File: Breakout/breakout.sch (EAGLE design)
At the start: 57 parts, among them Q1 16Mhz, U1 TPS63001DRCT, U11 XL

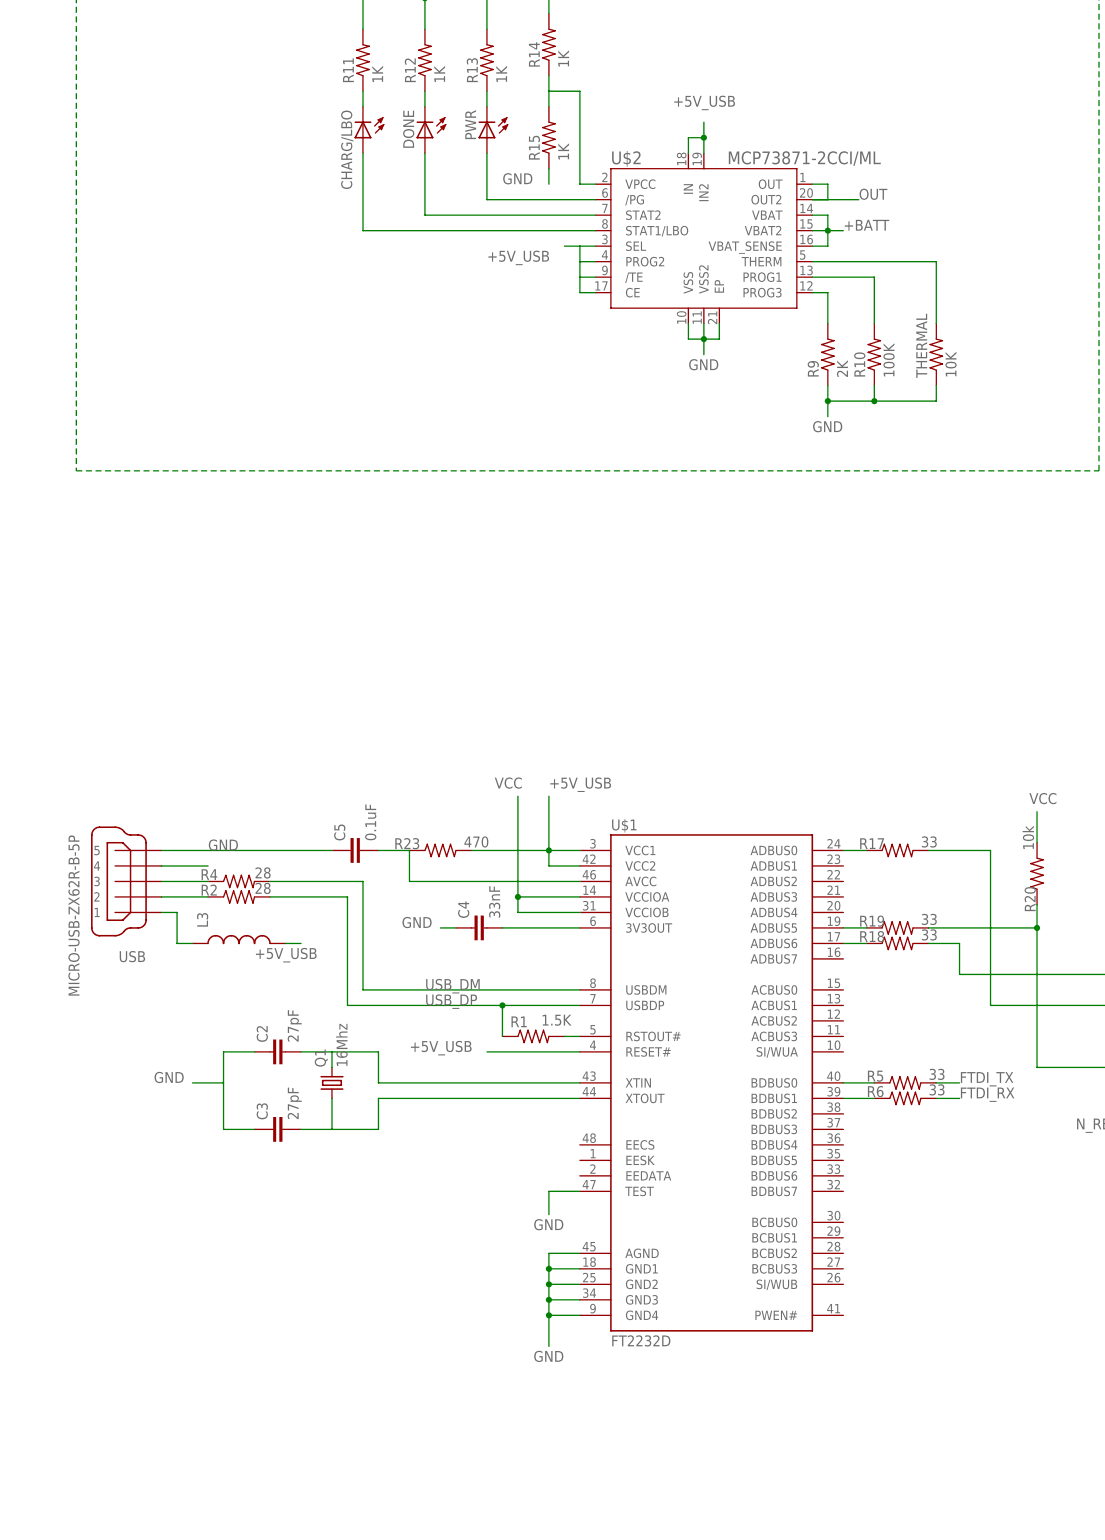
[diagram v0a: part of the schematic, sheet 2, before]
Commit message: Added EEPROM for FTDI chip
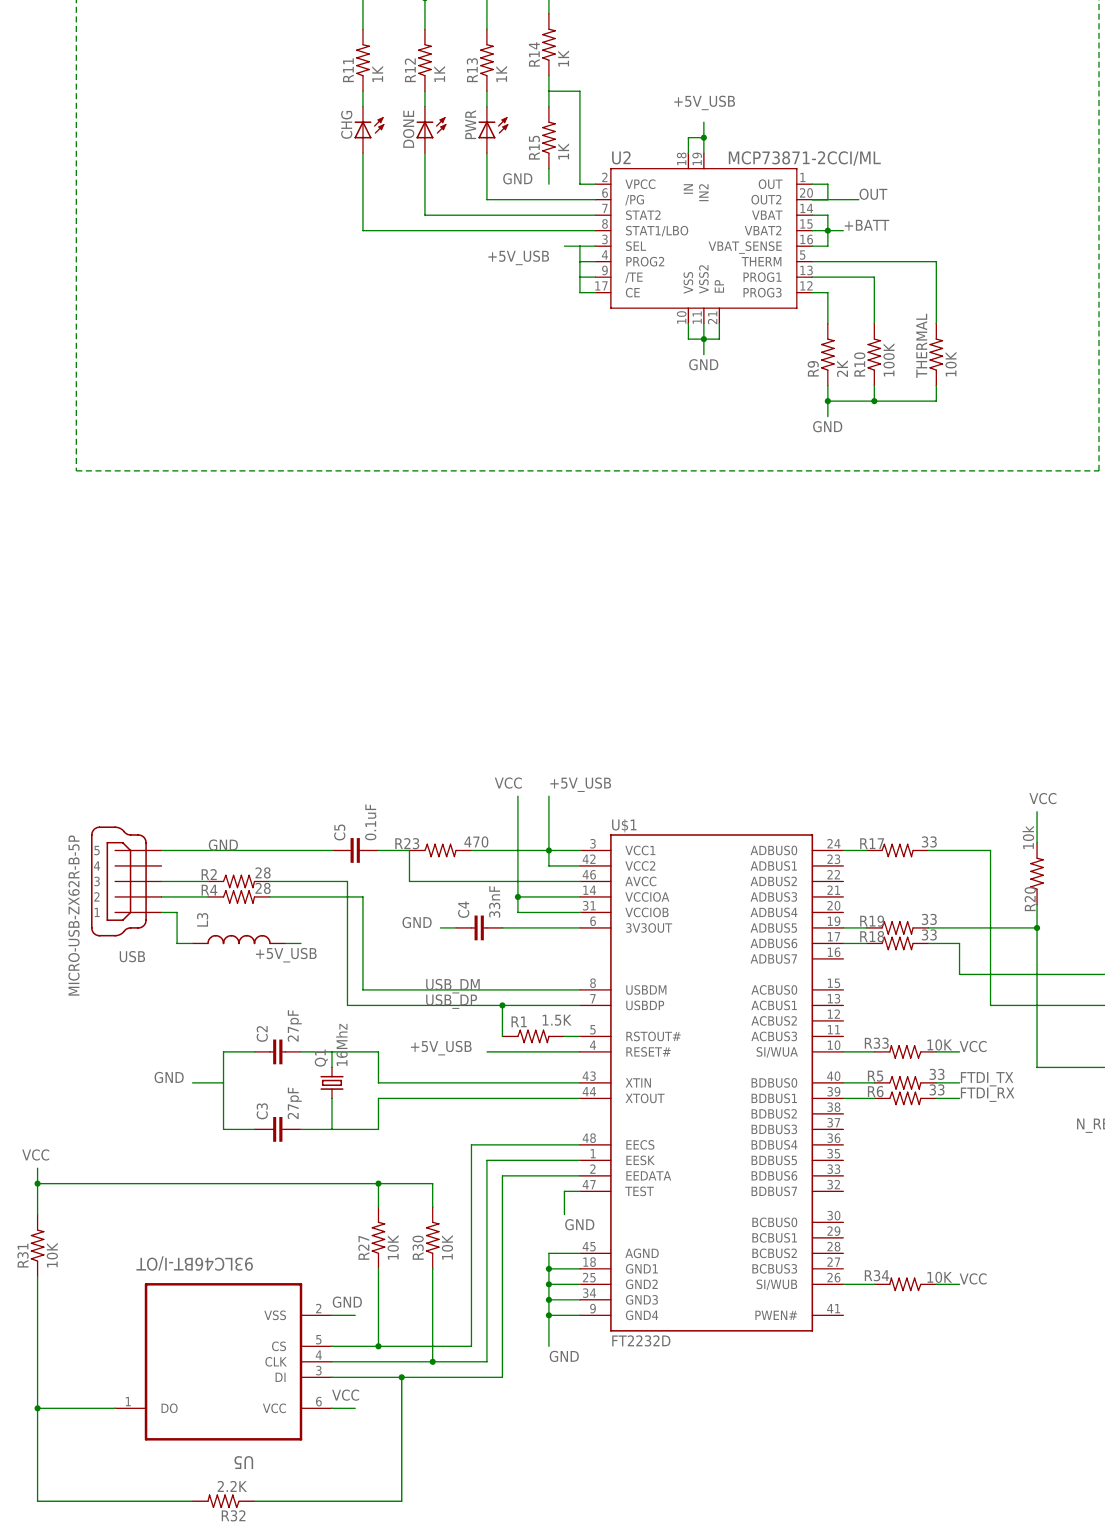
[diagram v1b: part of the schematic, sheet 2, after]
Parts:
- added R27, R30, R31, R33, R34: 10K, SparkFun-Passives:RESISTOR0402-RES
- added R32: 2.2K, SparkFun-Passives:RESISTOR0402-RES
- added U5: 93LC46BT-I/OT, Microchip_By_element14_Batch_1:93LC46BT-I/OT
- renumbered CHARG/LBO to CHG, U$2 to U2
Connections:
- new net N$16: R4.1, USB.2
- new net N$24: R2.1, USB.3
- new net N$54: R31.1, R32.2, U5.DO
- new net N$55: R33.2, U$1.SI/WUA
- new net N$56: R34.2, U$1.SI/WUB
- net GND: now also U5.VSS
- net N$39: now also R27.1, U$1.EECS, U5.CS; no longer USB.4
- net N$41: now also R30.1, U$1.EESK, U5.CLK; no longer R4.1, USB.3
- net N$42: now also R32.1, U$1.EEDATA, U5.DI; no longer R2.1, USB.2
- net VCC: now also R27.2, R30.2, R31.2, R33.1, U5.VCC
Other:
- moved on the sheet: R2, R4

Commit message: Temp Sensor added
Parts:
- added C7: .1uF, SparkFun-Capacitors:CAP0402-CAP
- added R35, R37: 0R, SparkFun-Passives:RESISTOR0603-RES
- added R36: 33K, SparkFun-Passives:RESISTOR0402-RES
- added U12: TMP006, SparkFun-DigitalIC:TMP006
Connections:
- new net GPIO_30: CC3200MOD.42_GPIO30, R35.1, U11.GPIO_30
- new net N$57: R35.2, R36.1, U12.!DRDY
- net GND: now also C7.1, U12.ADR0, U12.AGND, U12.DGND
- net GPIO_10: now also U12.SCL
- net GPIO_11: now also U12.SDA
- net N$14: now also C7.2, R36.2, R37.2, U12.ADR1, U12.V+; no longer CC3200MOD.42_GPIO30, U11.GPIO_30
- net VCC: now also R37.1
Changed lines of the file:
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@@
 <part name="R33" library="SparkFun-Passives" deviceset="RESISTOR" device="0402-RES" value="10K"/>
 <part name="R34" library="SparkFun-Passives" deviceset="RESISTOR" device="0402-RES" value="10K"/>
+<part name="U12" library="SparkFun-DigitalIC" deviceset="TMP006" device=""/>
+<part name="R35" library="SparkFun-Passives" deviceset="RESISTOR" device="0603-RES" value="0R"/>
+<part name="R36" library="SparkFun-Passives" deviceset="RESISTOR" device="0402-RES" value="33K"/>
+<part name="R37" library="SparkFun-Passives" deviceset="RESISTOR" device="0603-RES" value="0R"/>
+<part name="C7" library="SparkFun-Capacitors" deviceset="CAP" device="0402-CAP" value=".1uF"/>
 </parts>
 <sheets>
@@
 </segment>
 </net>
-<net name="N$14" class="0">
+<net name="GPIO_30" class="0">
 <segment>
 <pinref part="CC3200MOD" gate="G$1" pin="42_GPIO30"/>
@@
 <attribute name="VALUE" x="165.1" y="286.512" size="1.778" layer="96" rot="R180"/>
 </instance>
+<instance part="U12" gate="G$1" x="508" y="347.98" rot="R180"/>
+<instance part="R35" gate="G$1" x="469.9" y="340.36" rot="R90"/>
+<instance part="R36" gate="G$1" x="459.74" y="339.09" rot="R270"/>
+<instance part="R37" gate="G$1" x="532.13" y="342.9" rot="R180"/>
+<instance part="C7" gate="G$1" x="472.44" y="363.22" rot="R270"/>
 </instances>
 <busses>
@@
 <wire x1="63.5" y1="279.4" x2="67.31" y2="279.4" width="0.1524" layer="91"/>
 <label x="63.5" y="280.67" size="1.778" layer="95"/>
+</segment>
+<segment>
+<pinref part="U12" gate="G$1" pin="AGND"/>
+<wire x1="523.24" y1="353.06" x2="525.78" y2="353.06" width="0.1524" layer="91"/>
+<wire x1="525.78" y1="353.06" x2="525.78" y2="350.52" width="0.1524" layer="91"/>
+<wire x1="525.78" y1="350.52" x2="530.86" y2="350.52" width="0.1524" layer="91"/>
+<pinref part="U12" gate="G$1" pin="DGND"/>
+<wire x1="525.78" y1="350.52" x2="523.24" y2="350.52" width="0.1524" layer="91"/>
+<label x="530.86" y="350.52" size="1.778" layer="95"/>
+<junction x="525.78" y="350.52"/>
+</segment>
+<segment>
+<pinref part="U12" gate="G$1" pin="ADR0"/>
+<label x="482.6" y="353.06" size="1.778" layer="95"/>
+<wire x1="492.76" y1="353.06" x2="481.33" y2="353.06" width="0.1524" layer="91"/>
+<wire x1="481.33" y1="353.06" x2="481.33" y2="363.22" width="0.1524" layer="91"/>
+<pinref part="C7" gate="G$1" pin="1"/>
+<wire x1="481.33" y1="363.22" x2="477.52" y2="363.22" width="0.1524" layer="91"/>
 </segment>
 </net>
@@
 <label x="166.37" y="284.48" size="1.778" layer="95"/>
 </segment>
+<segment>
+<pinref part="R37" gate="G$1" pin="1"/>
+<wire x1="537.21" y1="342.9" x2="543.56" y2="342.9" width="0.1524" layer="91"/>
+<label x="543.56" y="342.9" size="1.778" layer="95"/>
+</segment>
 </net>
 <net name="N$9" class="0">
@@
 <pinref part="U$3" gate="G$1" pin="OE2"/>
 <wire x1="179.07" y1="320.04" x2="217.17" y2="320.04" width="0.1524" layer="91"/>
-<label x="191.77" y="342.9" size="1.778" layer="95"/>
+<label x="181.61" y="342.9" size="1.778" layer="95"/>
 <junction x="179.07" y="342.9"/>
 </segment>
@@
 <segment>
 <pinref part="R25" gate="G$1" pin="1"/>
-<wire x1="397.51" y1="307.34" x2="397.51" y2="302.26" width="0.1524" layer="91"/>
+<wire x1="397.51" y1="307.34" x2="397.51" y2="304.8" width="0.1524" layer="91"/>
 <label x="392.43" y="298.45" size="1.778" layer="95"/>
+<wire x1="397.51" y1="304.8" x2="397.51" y2="302.26" width="0.1524" layer="91"/>
+<wire x1="397.51" y1="309.88" x2="397.51" y2="304.8" width="0.1524" layer="91"/>
 </segment>
 </net>
@@
 <wire x1="440.69" y1="372.11" x2="440.69" y2="361.95" width="0.1524" layer="91"/>
 <label x="434.34" y="359.41" size="1.778" layer="95"/>
+</segment>
+<segment>
+<pinref part="U12" gate="G$1" pin="SCL"/>
+<wire x1="492.76" y1="342.9" x2="487.68" y2="342.9" width="0.1524" layer="91"/>
+<label x="477.52" y="342.9" size="1.778" layer="95"/>
 </segment>
 </net>
@@
 <wire x1="454.66" y1="369.57" x2="454.66" y2="361.95" width="0.1524" layer="91"/>
 <label x="450.85" y="359.41" size="1.778" layer="95"/>
+</segment>
+<segment>
+<pinref part="U12" gate="G$1" pin="SDA"/>
+<wire x1="492.76" y1="345.44" x2="487.68" y2="345.44" width="0.1524" layer="91"/>
+<label x="477.52" y="345.44" size="1.778" layer="95"/>
 </segment>
 </net>
@@
 </segment>
 </net>
+<net name="N$57" class="0">
+<segment>
+<pinref part="U12" gate="G$1" pin="!DRDY"/>
+<wire x1="492.76" y1="347.98" x2="469.9" y2="347.98" width="0.1524" layer="91"/>
+<wire x1="469.9" y1="347.98" x2="469.9" y2="345.44" width="0.1524" layer="91"/>
+<pinref part="R35" gate="G$1" pin="2"/>
+<pinref part="R36" gate="G$1" pin="1"/>
+<wire x1="469.9" y1="347.98" x2="459.74" y2="347.98" width="0.1524" layer="91"/>
+<wire x1="459.74" y1="347.98" x2="459.74" y2="344.17" width="0.1524" layer="91"/>
+<junction x="469.9" y="347.98"/>
+</segment>
+</net>
+<net name="GPIO_30" class="0">
+<segment>
+<pinref part="R35" gate="G$1" pin="1"/>
+<wire x1="469.9" y1="335.28" x2="469.9" y2="330.2" width="0.1524" layer="91"/>
+<label x="464.82" y="327.66" size="1.778" layer="95"/>
+</segment>
+</net>
+<net name="N$14" class="0">
+<segment>
+<pinref part="U12" gate="G$1" pin="V+"/>
+<wire x1="523.24" y1="342.9" x2="525.78" y2="342.9" width="0.1524" layer="91"/>
+<pinref part="R37" gate="G$1" pin="2"/>
+<pinref part="U12" gate="G$1" pin="ADR1"/>
+<wire x1="525.78" y1="342.9" x2="527.05" y2="342.9" width="0.1524" layer="91"/>
+<wire x1="492.76" y1="350.52" x2="474.98" y2="350.52" width="0.1524" layer="91"/>
+<wire x1="474.98" y1="350.52" x2="474.98" y2="335.28" width="0.1524" layer="91"/>
+<wire x1="474.98" y1="335.28" x2="525.78" y2="335.28" width="0.1524" layer="91"/>
+<wire x1="525.78" y1="335.28" x2="525.78" y2="342.9" width="0.1524" layer="91"/>
+<junction x="525.78" y="342.9"/>
+<pinref part="R36" gate="G$1" pin="2"/>
+<wire x1="459.74" y1="334.01" x2="459.74" y2="322.58" width="0.1524" layer="91"/>
+<wire x1="459.74" y1="322.58" x2="525.78" y2="322.58" width="0.1524" layer="91"/>
+<wire x1="525.78" y1="322.58" x2="525.78" y2="335.28" width="0.1524" layer="91"/>
+<junction x="525.78" y="335.28"/>
+<wire x1="474.98" y1="350.52" x2="467.36" y2="350.52" width="0.1524" layer="91"/>
+<wire x1="467.36" y1="350.52" x2="467.36" y2="363.22" width="0.1524" layer="91"/>
+<pinref part="C7" gate="G$1" pin="2"/>
+<wire x1="467.36" y1="363.22" x2="469.9" y2="363.22" width="0.1524" layer="91"/>
+</segment>
+</net>

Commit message: Finished WeBee
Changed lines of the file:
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@@
 <setting verticaltext="up"/>
 </settings>
-<grid distance="0.05" unitdist="inch" unit="inch" style="lines" multiple="1" display="no" altdistance="0.01" altunitdist="inch" altunit="inch"/>
+<grid distance="0.1" unitdist="inch" unit="inch" style="lines" multiple="1" display="no" altdistance="0.01" altunitdist="inch" altunit="inch"/>
 <layers>
 <layer number="1" name="Top" color="4" fill="1" visible="no" active="no"/>
@@
 <pinref part="R26" gate="G$1" pin="1"/>
 <wire x1="214.63" y1="374.65" x2="204.47" y2="374.65" width="0.1524" layer="91"/>
-</segment>
-<segment>
+<label x="198.12" y="373.38" size="1.778" layer="95"/>
+</segment>
+<segment>
